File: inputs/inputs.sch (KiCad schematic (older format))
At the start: 27 parts, among them P1 CONN_01X01, P10 CONN_01X01, P11 CONN_01X01, P12 CONN_01X01, P13 CONN_01X01, P2 CONN_01X01, P3 CONN_01X01, P4 CONN_01X05, P5 CONN_01X01, P6 CONN_01X01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

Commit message: inputs rev1, 13a_switch_x4 rev1
both hardware and firmware is working
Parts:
- C1: DIGIKEY 445-13057-1-ND -> 478-5230-1-ND
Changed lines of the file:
@@
 F 1 "10uF" H 4125 1450 50  0000 L CNN
 F 2 "Capacitors_SMD:C_1210_HandSoldering" H 4138 1400 50  0001 C CNN
-F 3 "http://www.digikey.com/product-detail/en/tdk-corporation/CGA6P3X8R1C106M250AB/445-13057-1-ND/3954723" H 4100 1550 50  0001 C CNN
-F 4 "445-13057-1-ND" H 4100 1550 60  0001 C CNN "DIGIKEY"
+F 3 "http://datasheets.avx.com/TPS.pdf" H 4100 1550 50  0001 C CNN
+F 4 "478-5230-1-ND" H 4100 1550 60  0001 C CNN "DIGIKEY"
 	1    4100 1550
 	1    0    0    -1

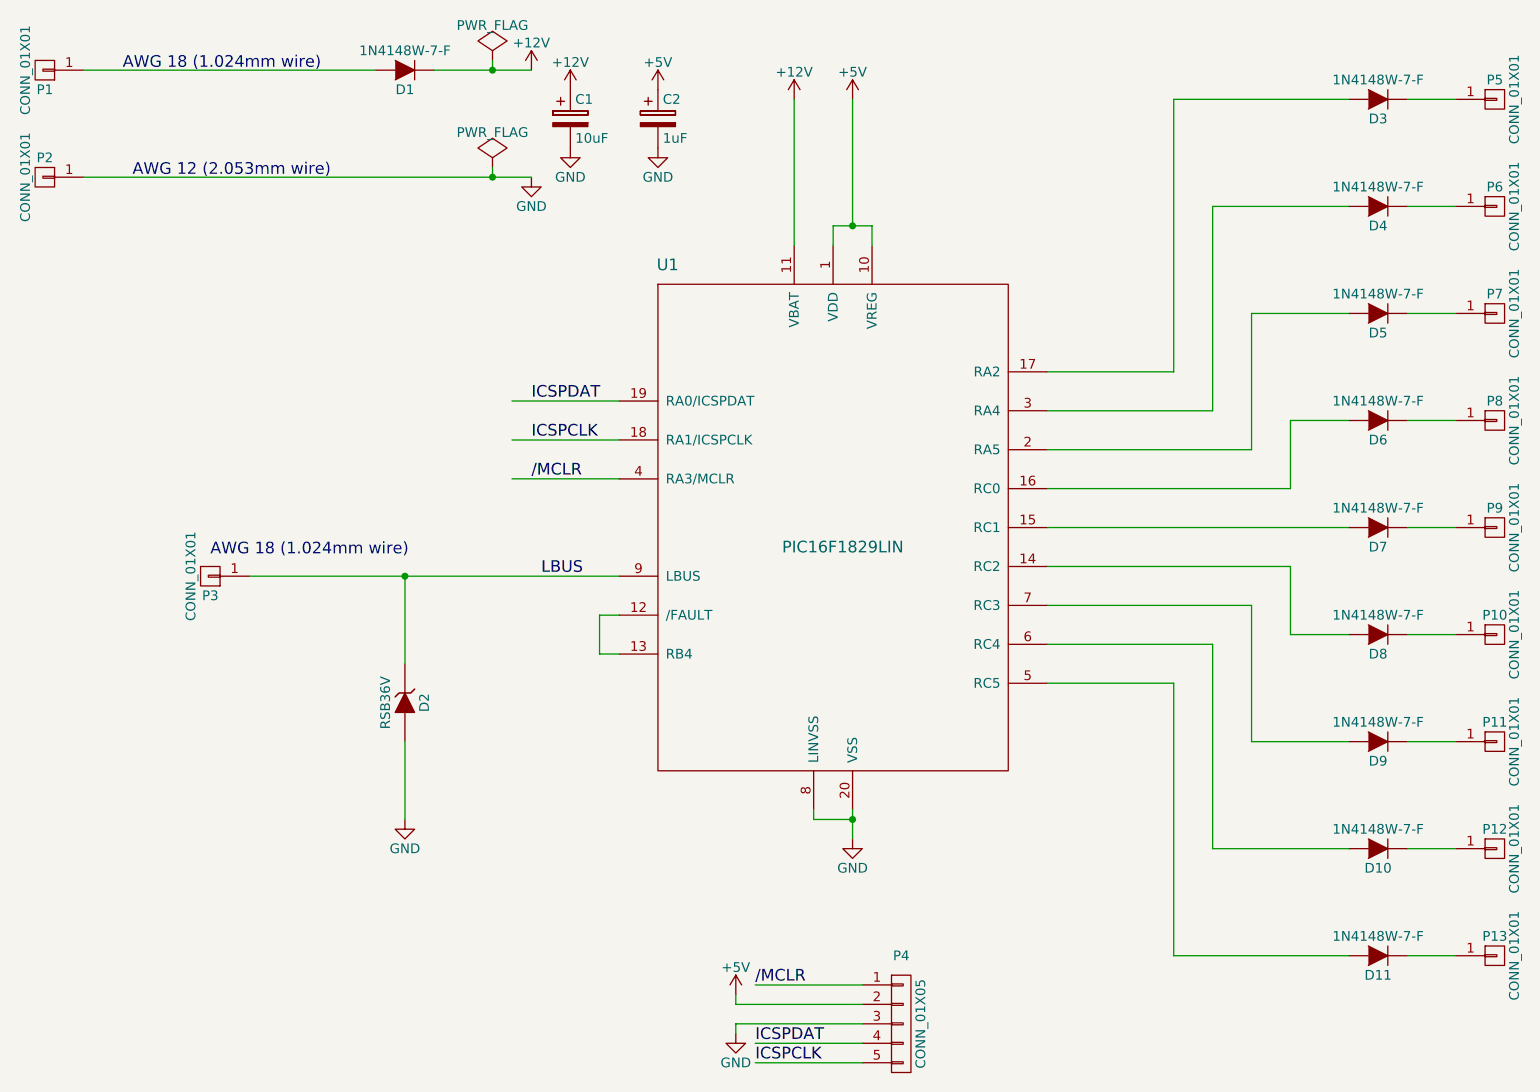
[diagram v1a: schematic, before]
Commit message: 8 inputs rev 2
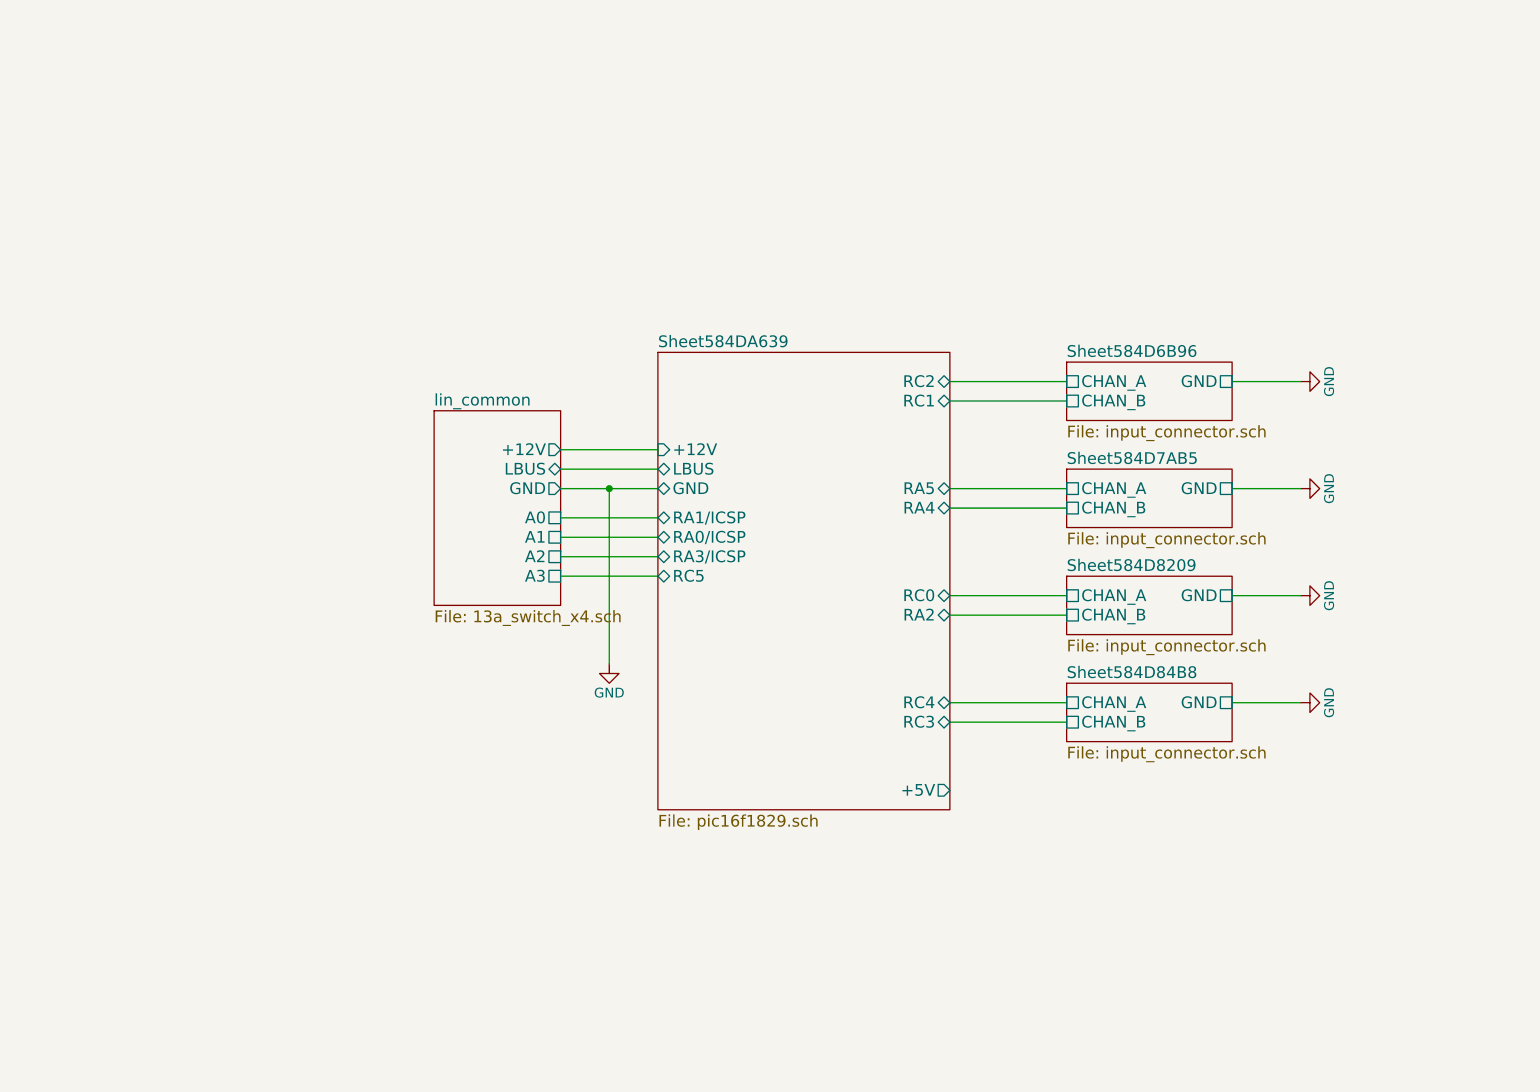
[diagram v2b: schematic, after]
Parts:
- removed C1: 10uF, Capacitors_SMD:C_1210_HandSoldering, symbol CP
- removed C2: 1uF, Capacitors_SMD:C_0805_HandSoldering, symbol CP
- removed D1, D10, D11, D3, D4, D5, D6, D7, D8, D9: 1N4148W-7-F, Diodes_SMD:SOD-123, symbol D
- removed D2: RSB36V, Diodes_SMD:SOD-323_HandSoldering, symbol ZENER
- removed P1, P10, P11, P12, P13, P2, P3, P5, P6, P7, P8, P9: CONN_01X01, footprints:wire_awg_18, symbol CONN_01X01
- removed P4: CONN_01X05, Pin_Headers:Pin_Header_Angled_1x05, symbol CONN_01X05
- removed U1: PIC16F1829LIN, Housings_SSOP:SSOP-20_5.3x7.2mm_Pitch0.65mm, symbol PIC16F1829LIN
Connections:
- net labels removed: +12V, +5V, /MCLR, ICSPCLK, ICSPDAT, LBUS
- wire segments 63 -> 20
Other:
- note removed: "AWG 12 (2.053mm wire)"
- note removed: "AWG 18 (1.024mm wire)"
